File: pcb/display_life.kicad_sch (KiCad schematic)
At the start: 22 parts

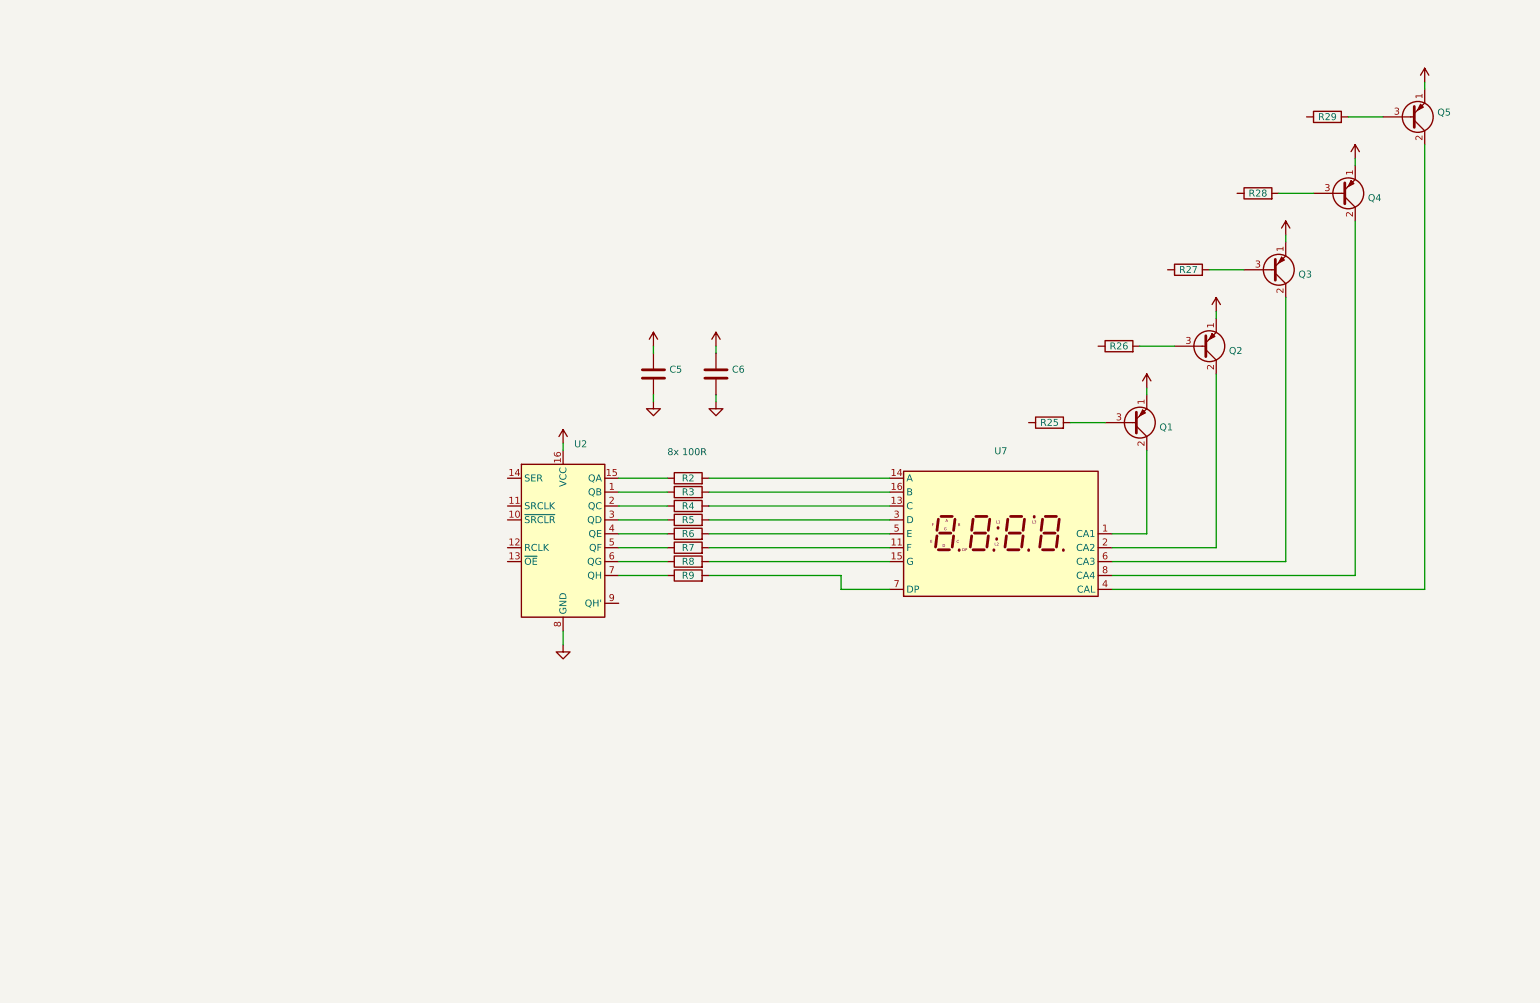
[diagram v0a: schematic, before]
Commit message: test layout and first traces
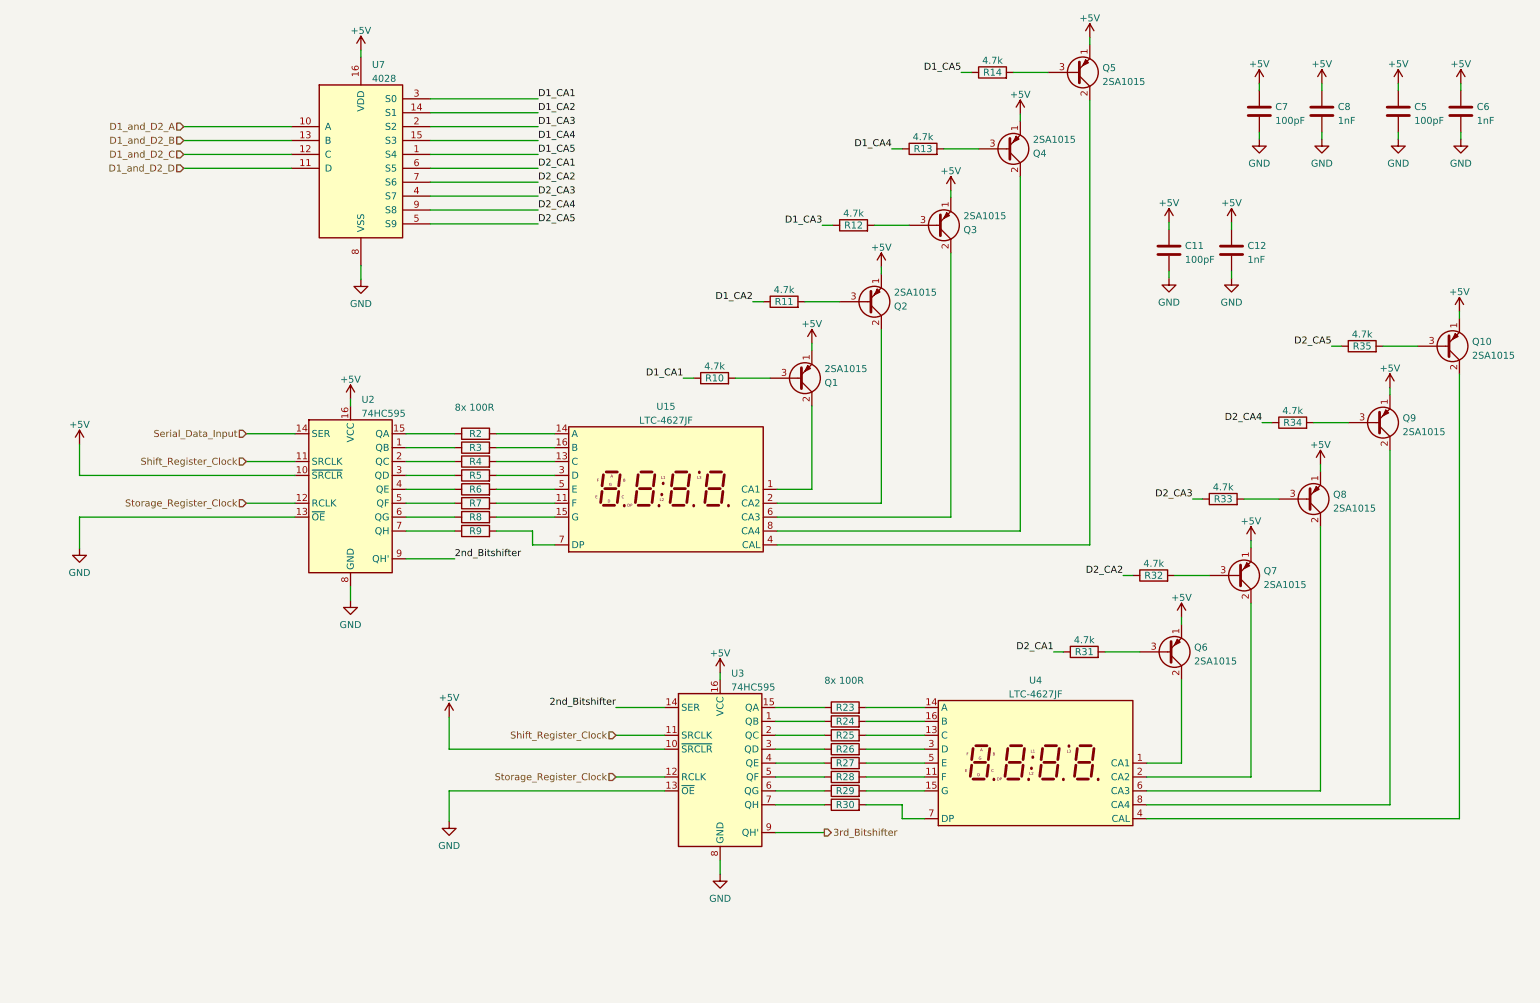
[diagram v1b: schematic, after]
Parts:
- added C11, C7: 100pF, Capacitor_THT:C_Disc_D3.8mm_W2.6mm_P2.50mm, symbol Device:C
- added C12, C8: 1nF, Capacitor_THT:C_Disc_D3.8mm_W2.6mm_P2.50mm, symbol Device:C
- added Q10, Q6, Q7, Q8, Q9: 2SA1015, Package_TO_SOT_THT:TO-92_Wide, symbol Transistor_BJT:2SA1015
- added R23, R24, R25, R26, R27, R28, R29, R30: 100R, Resistor_THT:R_Axial_DIN0207_L6.3mm_D2.5mm_P7.62mm_Horizontal, symbol Device:R
- added R31, R32, R33, R34, R35: 4.7k, Resistor_THT:R_Axial_DIN0207_L6.3mm_D2.5mm_P7.62mm_Horizontal, symbol Device:R
- added U3: 74HC595, Package_DIP:DIP-16_W7.62mm_LongPads, symbol 74xx:74HC595
- added U4: LTC-4627JF, Display_7Segment:LTC-4627Jx, symbol Display_Character:LTC-4627JF
- added U7: 4028, Package_DIP:DIP-16_W7.62mm_LongPads, symbol 4xxx:4028
- C5: value (none) -> 100pF; footprint (none) -> Capacitor_THT:C_Disc_D3.8mm_W2.6mm_P2.50mm
- C6: value (none) -> 1nF; footprint (none) -> Capacitor_THT:C_Disc_D3.8mm_W2.6mm_P2.50mm
- Q1, Q2, Q3, Q4, Q5: value (none) -> 2SA1015; footprint (none) -> Package_TO_SOT_THT:TO-92_Wide
- R10: renamed from R25; value (none) -> 4.7k; footprint (none) -> Resistor_THT:R_Axial_DIN0207_L6.3mm_D2.5mm_P7.62mm_Horizontal
- R11: renamed from R26; value (none) -> 4.7k; footprint (none) -> Resistor_THT:R_Axial_DIN0207_L6.3mm_D2.5mm_P7.62mm_Horizontal
- R12: renamed from R27; value (none) -> 4.7k; footprint (none) -> Resistor_THT:R_Axial_DIN0207_L6.3mm_D2.5mm_P7.62mm_Horizontal
- R13: renamed from R28; value (none) -> 4.7k; footprint (none) -> Resistor_THT:R_Axial_DIN0207_L6.3mm_D2.5mm_P7.62mm_Horizontal
- R14: renamed from R29; value (none) -> 4.7k; footprint (none) -> Resistor_THT:R_Axial_DIN0207_L6.3mm_D2.5mm_P7.62mm_Horizontal
- R2, R3, R4, R5, R6, R7, R8, R9: value (none) -> 100R; footprint (none) -> Resistor_THT:R_Axial_DIN0207_L6.3mm_D2.5mm_P7.62mm_Horizontal
- U15: renamed from U7; value (none) -> LTC-4627JF; footprint (none) -> Display_7Segment:LTC-4627Jx
- U2: value (none) -> 74HC595; footprint (none) -> Package_DIP:DIP-16_W7.62mm_LongPads
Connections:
- net +5V: now also U2.10 (~{SRCLR}), C11.1, C12.1, C7.1, C8.1, Q10.1 (E), Q6.1 (E), Q7.1 (E), Q8.1 (E), Q9.1 (E), U3.10 (~{SRCLR}), U3.16 (VCC), U7.16 (VDD)
- net GND: now also U2.13 (~{OE}), C11.2, C12.2, C7.2, C8.2, U3.13 (~{OE}), U3.8 (GND), U7.8 (VSS)
- net D1_CA4: now reaches R13.1
- net D1_CA4: now also U7.15 (S3)
- net D1_CA5: now reaches R14.1
- net D1_CA5: now also U7.1 (S4)
- net D1_CA2: now reaches R11.1
- net D1_CA2: now also U7.14 (S1)
- net Shift_Register_Clock: now reaches U2.11 (SRCLK)
- net Shift_Register_Clock: now also U3.11 (SRCLK)
- net Storage_Register_Clock: now reaches U2.12 (RCLK)
- net Storage_Register_Clock: now also U3.12 (RCLK)
- net Serial_Data_Input: now reaches U2.14 (SER)
- net 2nd_Bitshifter: now reaches U2.9 (QH')
- net 2nd_Bitshifter: now also U3.14 (SER)
- net D1_CA1: now reaches R10.1
- net D1_CA1: now also U7.3 (S0)
- net D1_CA3: now reaches R12.1
- net D1_CA3: now also U7.2 (S2)
- new net: R27.1, U3.4 (QE)
- new net: R27.2, U4.5 (E)
- new net: Q9.2 (C), U4.8 (CA4)
- new net: Q9.3 (B), R34.2
- new net: R25.1, U3.2 (QC)
- new net: R25.2, U4.13 (C)
- new net: R24.1, U3.1 (QB)
- new net: R23.1, U3.15 (QA)
- new net: R26.1, U3.3 (QD)
- new net: R28.1, U3.5 (QF)
- new net: R29.1, U3.6 (QG)
- new net: R30.1, U3.7 (QH)
- new net: Q10.3 (B), R35.2
- new net: Q7.2 (C), U4.2 (CA2)
- new net: Q7.3 (B), R32.2
- new net: Q8.2 (C), U4.6 (CA3)
- new net: Q8.3 (B), R33.2
- new net: Q6.2 (C), U4.1 (CA1)
- new net: R28.2, U4.11 (F)
- new net: R23.2, U4.14 (A)
- new net: R29.2, U4.15 (G)
- new net: R24.2, U4.16 (B)
- new net: R26.2, U4.3 (D)
- new net: Q10.2 (C), U4.4 (CAL)
- new net: R30.2, U4.7 (DP)
- new net: Q6.3 (B), R31.2
- new net 3rd_Bitshifter: U3.9 (QH')
- new net D1_and_D2_A: U7.10 (A)
- new net D1_and_D2_B: U7.13 (B)
- new net D1_and_D2_C: U7.12 (C)
- new net D1_and_D2_D: U7.11 (D)
- new net D2_CA1: R31.1, U7.6 (S5)
- new net D2_CA2: R32.1, U7.7 (S6)
- new net D2_CA3: R33.1, U7.4 (S7)
- new net D2_CA4: R34.1, U7.9 (S8)
- new net D2_CA5: R35.1, U7.5 (S9)
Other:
- moved on the sheet: C5, C6, Q1, Q2, Q3, Q4, Q5, R10, R11, R12, R13, R14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

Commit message: new layout test
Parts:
- renumbered U7 to U4, U15 to U5, U4 to U6
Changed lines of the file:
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@@
   (symbol (lib_id "Display_Character:LTC-4627JF") (at 125.476 101.092 0) (unit 1)
     (in_bom yes) (on_board yes) (fields_autoplaced)
-    (property "Reference" "U15" (id 0) (at 125.476 85.9622 0))
+    (property "Reference" "U5" (id 0) (at 125.476 85.9622 0))
     (property "Value" "LTC-4627JF" (id 1) (at 125.476 88.4991 0))
     (property "Footprint" "Display_7Segment:LTC-4627Jx" (id 2) (at 125.476 113.792 0)
@@
   (symbol (lib_id "Display_Character:LTC-4627JF") (at 193.04 151.13 0) (unit 1)
     (in_bom yes) (on_board yes) (fields_autoplaced)
-    (property "Reference" "U4" (id 0) (at 193.04 136.0002 0))
+    (property "Reference" "U6" (id 0) (at 193.04 136.0002 0))
     (property "Value" "LTC-4627JF" (id 1) (at 193.04 138.5371 0))
     (property "Footprint" "Display_7Segment:LTC-4627Jx" (id 2) (at 193.04 163.83 0)
@@
   (symbol (lib_id "4xxx:4028") (at 69.723 39.878 0) (unit 1)
     (in_bom yes) (on_board yes) (fields_autoplaced)
-    (property "Reference" "U7" (id 0) (at 71.7424 23.4782 0)
-      (effects (font (size 1.27 1.27)) (justify left))
-    )
+    (property "Reference" "U4" (id 0) (at 71.7424 23.4782 0)
+      (effects (font (size 1.27 1.27)) (justify left))
+    )

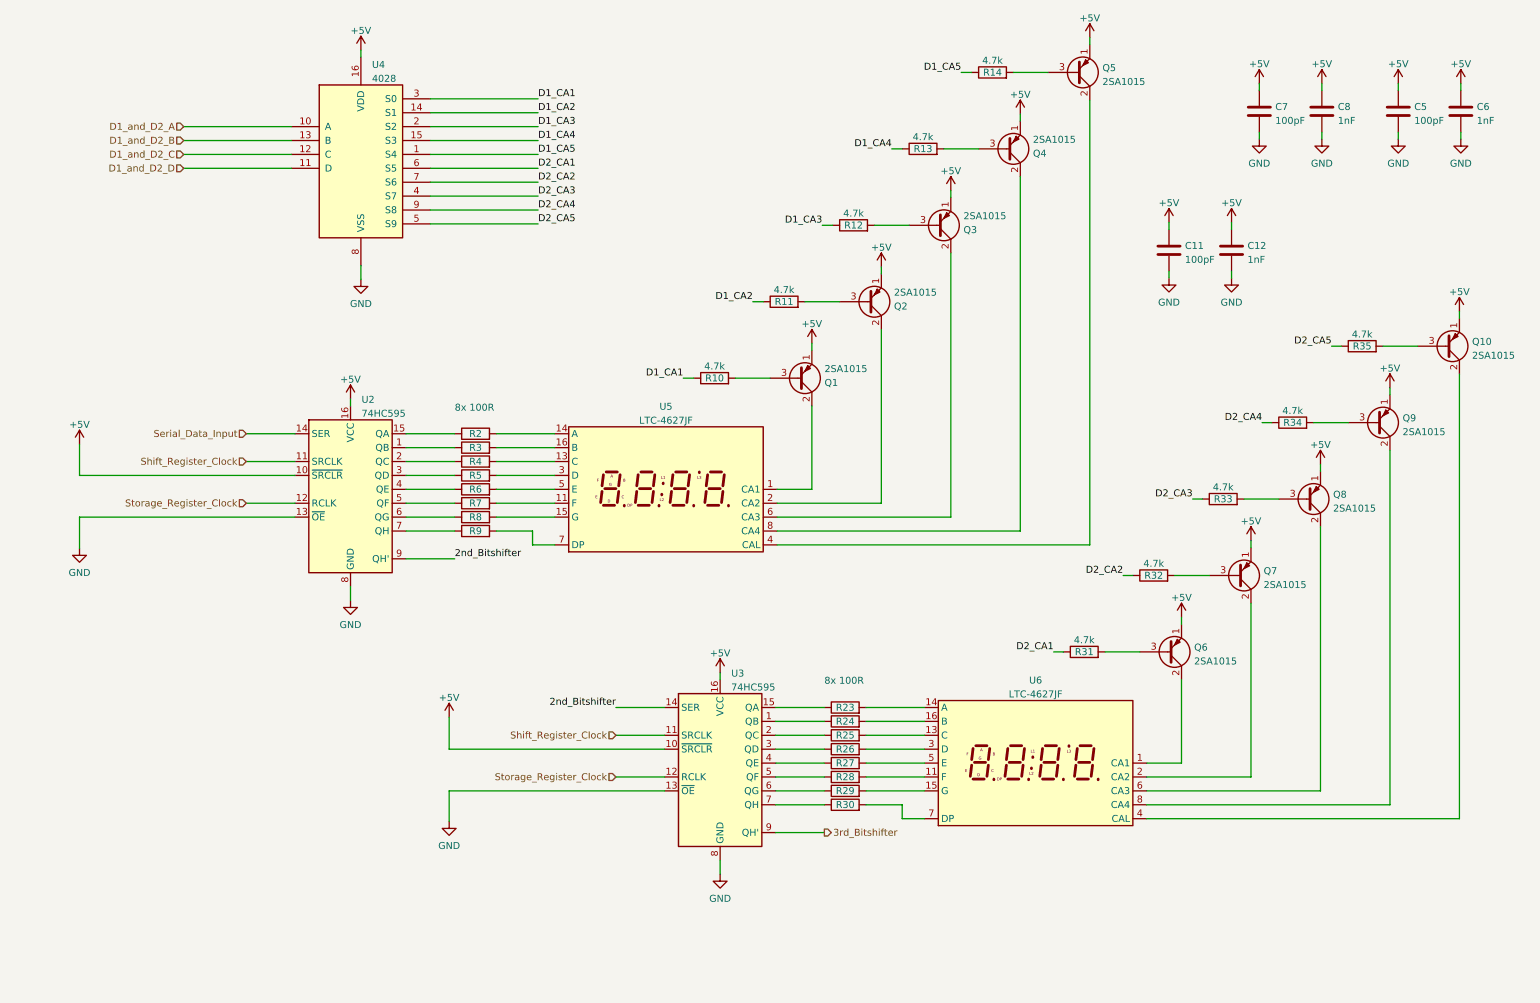
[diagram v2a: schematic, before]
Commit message: fewer parts and reduced to prototyping board with more logic analyzer pins
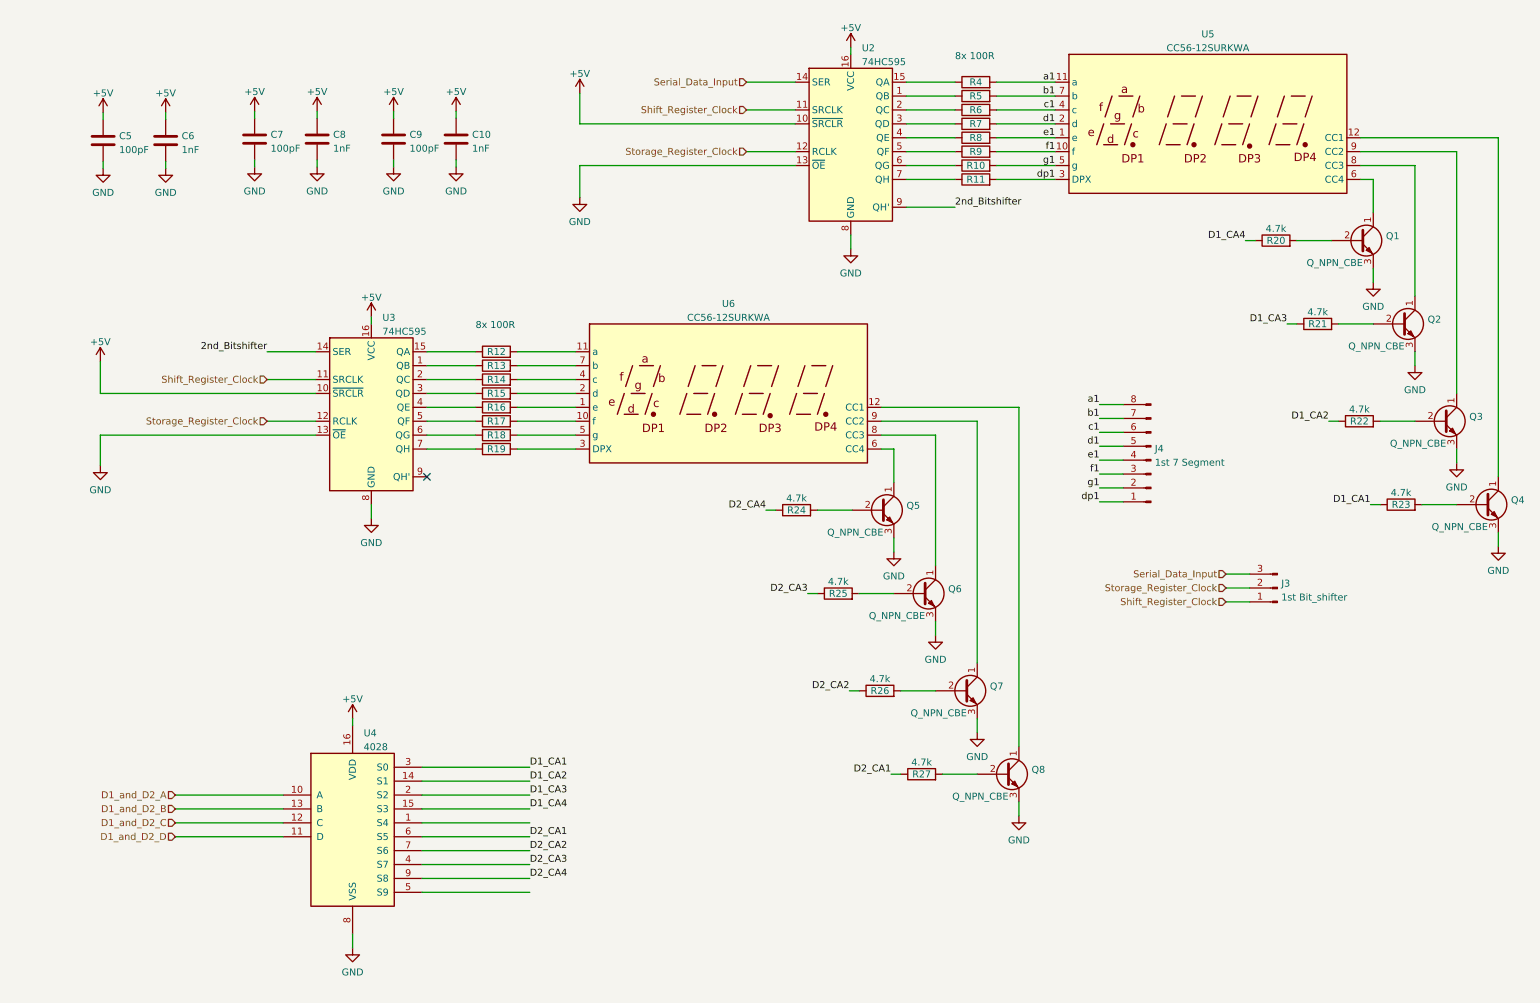
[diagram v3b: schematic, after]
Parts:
- removed Q1, Q10, Q2, Q3, Q4, Q5, Q6, Q7, Q8, Q9: 2SA1015, Package_TO_SOT_THT:TO-92_Wide, symbol Transistor_BJT:2SA1015
- removed R10, R31, R32, R33, R34, R35: 4.7k, Resistor_THT:R_Axial_DIN0207_L6.3mm_D2.5mm_P7.62mm_Horizontal, symbol Device:R
- removed U5, U6: LTC-4627JF, Display_7Segment:LTC-4627Jx, symbol Display_Character:LTC-4627JF
- added J3: 1st Bit_shifter, Connector_PinHeader_2.54mm:PinHeader_1x03_P2.54mm_Vertical, symbol Connector:Conn_01x03_Male
- added J4: 1st 7 Segment, Connector_PinHeader_2.54mm:PinHeader_1x08_P2.54mm_Vertical, symbol Connector:Conn_01x08_Male
- added Q1, Q2, Q3, Q4, Q5, Q6, Q7, Q8: Q_NPN_CBE, Package_TO_SOT_THT:TO-92_Inline_Wide, symbol Device:Q_NPN_CBE
- added R24, R25, R26, R27: 4.7k, Resistor_THT:R_Axial_DIN0207_L6.3mm_D2.5mm_P7.62mm_Horizontal, symbol Device:R
- added U5, U6: CC56-12SURKWA, Display_7Segment:CA56-12SURKWA, symbol Display_Character:CC56-12SURKWA
- renumbered C6 to C10, C11 to C5, C12 to C6, C5 to C9, R8 to R10, R9 to R11, R23 to R12, R24 to R13, R25 to R14, R26 to R15, R27 to R16, R28 to R17, R29 to R18, R30 to R19, R14 to R20, R13 to R21, R12 to R22, R11 to R23, R2 to R4, R3 to R5, R4 to R6, R5 to R7, R6 to R8, R7 to R9
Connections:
- net D1_CA1: now also R23.1
- net D1_CA2: now also R22.1; no longer R23.1
- net D1_CA3: now also R21.1; no longer R22.1
- net D1_CA4: now also R20.1; no longer R21.1
- net D2_CA1: now also R27.1
- net D2_CA2: now also R26.1
- net D2_CA3: now also R25.1
- net D2_CA4: now also R24.1
- net GND: now also Q1.3 (E), Q2.3 (E), Q3.3 (E), Q4.3 (E), Q5.3 (E), Q6.3 (E), Q7.3 (E), Q8.3 (E)
- net Serial_Data_Input: now also J3.3 (Pin_3)
- net Shift_Register_Clock: now also J3.1 (Pin_1)
- net Storage_Register_Clock: now also J3.2 (Pin_2)
- net at R16.2: now also U6.1 (e)
- net at R21.2: now also Q2.2 (B)
- net at R20.2: now also Q1.2 (B)
- net at R14.2: now also U6.4 (c)
- net f1: now reaches R9.2
- net f1: now also J4.3 (Pin_3), U5.10 (f)
- net c1: now reaches R6.2
- net c1: now also J4.6 (Pin_6), U5.4 (c)
- net a1: now reaches R4.2
- net a1: now also J4.8 (Pin_8), U5.11 (a)
- net g1: now reaches R10.2
- net g1: now also J4.2 (Pin_2), U5.5 (g)
- net b1: now reaches R5.2
- net b1: now also J4.7 (Pin_7), U5.7 (b)
- net d1: now reaches R7.2
- net d1: now also J4.5 (Pin_5), U5.2 (d)
- net e1: now reaches R8.2
- net e1: now also J4.4 (Pin_4), U5.1 (e)
- net dp1: now reaches R11.2
- net dp1: now also J4.1 (Pin_1), U5.3 (DPX)
- net at R23.2: now also Q4.2 (B)
- net at R22.2: now also Q3.2 (B)
- net at R17.2: now also U6.10 (f)
- net at R12.2: now also U6.11 (a)
- net at R18.2: now also U6.5 (g)
- net at R13.2: now also U6.7 (b)
- net at R15.2: now also U6.2 (d)
- net at R19.2: now also U6.3 (DPX)
- net 3rd_Bitshifter: no longer names the net of U3.9 (QH')
- net D1_CA5: no longer names the net of U4.1 (S4)
- net D1_CA5: no longer R20.1
- net D2_CA5: no longer names the net of U4.5 (S9)
- new net: Q3.1 (C), U5.9 (CC2)
- new net: Q5.2 (B), R24.2
- new net: Q4.1 (C), U5.12 (CC1)
- new net: Q7.1 (C), U6.9 (CC2)
- new net: Q7.2 (B), R26.2
- new net: Q6.2 (B), R25.2
- new net: Q5.1 (C), U6.6 (CC4)
- new net: Q1.1 (C), U5.6 (CC4)
- new net: Q2.1 (C), U5.8 (CC3)
- new net: Q8.1 (C), U6.12 (CC1)
- new net: Q6.1 (C), U6.8 (CC3)
- new net: Q8.2 (B), R27.2
- no-connect marks 0 -> 1
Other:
- moved on the sheet: C10, C5, C6, C7, C8, C9, R10, R11, R12, R13, R14, R15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
